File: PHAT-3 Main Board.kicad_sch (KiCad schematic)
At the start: 30 parts, among them P1 Power Terminal Block, P2 Power Terminal Block, P3 Power Terminal Block, P4 Power Terminal Block, Q1 IRLZ44N, SW1 SW_Push_SPDT, U1 AHT21, U10 Logic Level Converter, U2 ESP32-S3 Dual-core SX1262, U3 GY-68 BMP180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

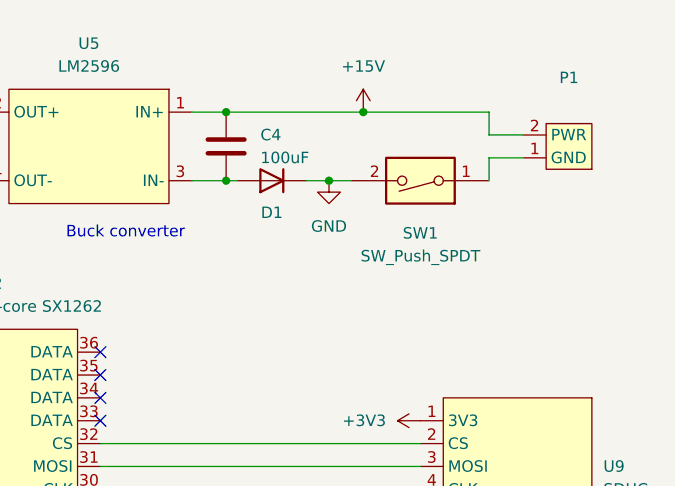
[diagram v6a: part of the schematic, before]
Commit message: Updated Switch and Resistor Placement
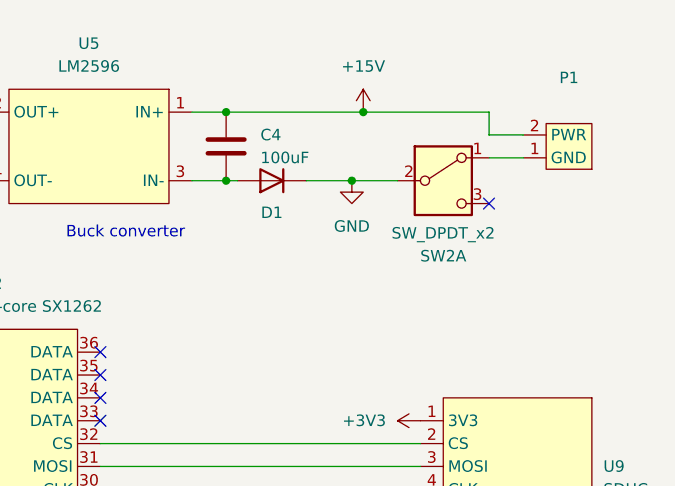
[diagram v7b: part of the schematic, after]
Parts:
- removed SW1: SW_Push_SPDT, Button_Switch_THT:SW_DIP_SPSTx01_Slide_9.78x4.72mm_W7.62mm_P2.54mm, symbol Switch:SW_DIP_x01
- added SW2: SW_DPDT_x2, Button_Switch_THT:SW_Slide-03_Wuerth-WS-SLTV_10x2.5x6.4_P2.54mm, symbol Switch:SW_DPDT_x2
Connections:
- net GND: now also SW2.2 (B)
- net at P1.1 (GND): now also SW2.1 (A)
- no-connect marks 31 -> 32
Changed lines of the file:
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@@
 	)
 	(junction
+		(at 204.47 46.99)
+		(diameter 0)
+		(color 0 0 0 0)
+	)
+	(junction
 		(at 102.87 99.06)
 		(diameter 0)
@@
 	)
 	(junction
-		(at 201.93 46.99)
-		(diameter 0)
-		(color 0 0 0 0)
-	)
-	(junction
 		(at 95.25 96.52)
 		(diameter 0)
@@
 	)
 	(no_connect
+		(at 219.71 49.53)
+	)
+	(no_connect
 		(at 123.19 138.43)
 	)
@@
 	(wire
 		(pts
+			(xy 219.71 44.45) (xy 223.52 44.45)
+		)
+		(stroke
+			(width 0)
+			(type default)
+		)
+	)
+	(wire
+		(pts
 			(xy 107.95 53.34) (xy 107.95 71.12)
 		)
@@
 	(wire
 		(pts
-			(xy 199.39 46.99) (xy 201.93 46.99)
+			(xy 199.39 46.99) (xy 204.47 46.99)
 		)
 		(stroke
@@
 	(wire
 		(pts
-			(xy 219.71 44.45) (xy 223.52 44.45)
-		)
-		(stroke
-			(width 0)
-			(type default)
-		)
-	)
-	(wire
-		(pts
 			(xy 133.35 99.06) (xy 133.35 114.3)
 		)
@@
 	(wire
 		(pts
-			(xy 201.93 46.99) (xy 204.47 46.99)
-		)
-		(stroke
-			(width 0)
-			(type default)
-		)
-	)
-	(wire
-		(pts
 			(xy 135.89 96.52) (xy 152.4 96.52)
 		)
@@
 	(wire
 		(pts
-			(xy 219.71 46.99) (xy 219.71 44.45)
-		)
-		(stroke
-			(width 0)
-			(type default)
-		)
-	)
-	(wire
-		(pts
 			(xy 119.38 73.66) (xy 119.38 93.98)
 		)
@@
 	(wire
 		(pts
+			(xy 204.47 46.99) (xy 209.55 46.99)
+		)
+		(stroke
+			(width 0)
+			(type default)
+		)
+	)
+	(wire
+		(pts
 			(xy 176.53 78.74) (xy 212.09 78.74)
 		)
@@
 	)
 	(symbol
+		(lib_id "Switch:SW_DPDT_x2")
+		(at 214.63 46.99 0)
+		(unit 1)
+		(exclude_from_sim no)
+		(in_bom yes)
+		(on_board yes)
+		(dnp no)
+		(property "Reference" "SW2"
+			(at 214.63 55.372 0)
+			(effects
+				(font
+					(size 1.27 1.27)
+				)
+			)
+		)
+		(property "Value" "SW_DPDT_x2"
+			(at 214.63 52.832 0)
+			(effects
+				(font
+					(size 1.27 1.27)
+				)
+			)
+		)
+		(property "Footprint" "Button_Switch_THT:SW_Slide-03_Wuerth-WS-SLTV_10x2.5x6.4_P2.54mm"
+			(at 214.63 46.99 0)
+			(effects
+				(font
+					(size 1.27 1.27)
+				)
+				(hide yes)
+			)
+		)
+		(property "Datasheet" "~"
+			(at 214.63 46.99 0)
+			(effects
+				(font
+					(size 1.27 1.27)
+				)
+				(hide yes)
+			)
+		)
+		(property "Description" "Switch, dual pole double throw, separate symbols"
+			(at 214.63 46.99 0)
+			(effects
+				(font
+					(size 1.27 1.27)
+				)
+				(hide yes)
+			)
+		)
+		(pin "5"
+		)
+		(pin "1"
+		)
+		(pin "6"
+		)
+		(pin "4"
+		)
+		(pin "3"
+		)
+		(pin "2"
+		)
+		(instances
+			(project ""
+				(path "/da389c8a-9ca2-41c4-a7eb-3ce46ba4333b"
+					(reference "SW2")
+					(unit 1)
+				)
+			)
+		)
+	)
+	(symbol
 		(lib_id "Footprint Library:uCAM-III")
 		(at 113.03 50.8 90)
@@
 	)
 	(symbol
-		(lib_id "Switch:SW_DIP_x01")
-		(at 212.09 46.99 180)
-		(unit 1)
-		(exclude_from_sim no)
-		(in_bom yes)
-		(on_board yes)
-		(dnp no)
-		(property "Reference" "SW1"
-			(at 212.09 52.832 0)
-			(effects
-				(font
-					(size 1.27 1.27)
-				)
-			)
-		)
-		(property "Value" "SW_Push_SPDT"
-			(at 212.09 55.372 0)
-			(effects
-				(font
-					(size 1.27 1.27)
-				)
-			)
-		)
-		(property "Footprint" "Button_Switch_THT:SW_DIP_SPSTx01_Slide_9.78x4.72mm_W7.62mm_P2.54mm"
-			(at 212.09 46.99 0)
-			(effects
-				(font
-					(size 1.27 1.27)
-				)
-				(hide yes)
-			)
-		)
-		(property "Datasheet" "~"
-			(at 212.09 46.99 0)
-			(effects
-				(font
-					(size 1.27 1.27)
-				)
-				(hide yes)
-			)
-		)
-		(property "Description" "1x DIP Switch, Single Pole Single Throw (SPST) switch, small symbol"
-			(at 212.09 46.99 0)
-			(effects
-				(font
-					(size 1.27 1.27)
-				)
-				(hide yes)
-			)
-		)
-		(pin "1"
-		)
-		(pin "2"
-		)
-		(instances
-			(project ""
-				(path "/da389c8a-9ca2-41c4-a7eb-3ce46ba4333b"
-					(reference "SW1")
-					(unit 1)
-				)
-			)
-		)
-	)
-	(symbol
 		(lib_id "power:+3V3")
 		(at 102.87 106.68 180)
@@
 	(symbol
 		(lib_id "power:GND")
-		(at 201.93 46.99 0)
+		(at 204.47 46.99 0)
 		(unit 1)
 		(exclude_from_sim no)
@@
 		(fields_autoplaced yes)
 		(property "Reference" "#PWR031"
-			(at 201.93 53.34 0)
+			(at 204.47 53.34 0)
 			(effects
 				(font
@@
 		)
 		(property "Value" "GND"
-			(at 201.93 52.07 0)
+			(at 204.47 52.07 0)
 			(effects
 				(font
@@
 		)
 		(property "Footprint" ""
-			(at 201.93 46.99 0)
+			(at 204.47 46.99 0)
 			(effects
 				(font
@@
 		)
 		(property "Datasheet" ""
-			(at 201.93 46.99 0)
+			(at 204.47 46.99 0)
 			(effects
 				(font
@@
 		)
 		(property "Description" "Power symbol creates a global label with name \"GND\" , ground"
-			(at 201.93 46.99 0)
+			(at 204.47 46.99 0)
 			(effects
 				(font

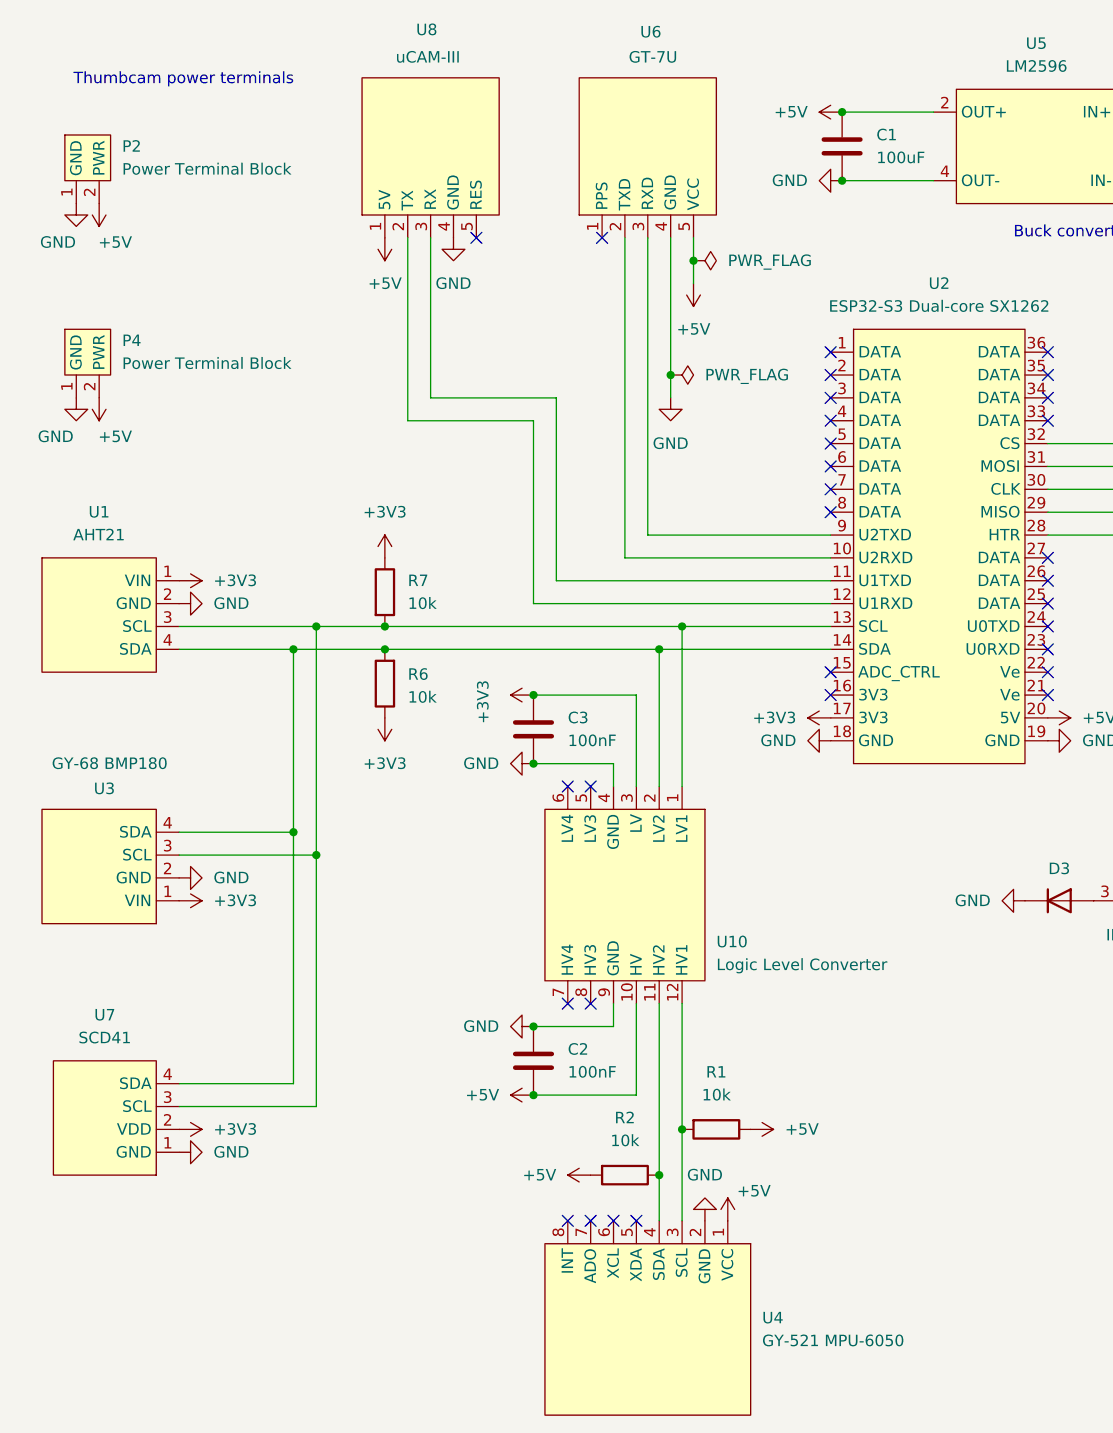
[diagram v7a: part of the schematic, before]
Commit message: Changed UART and I2C Pins
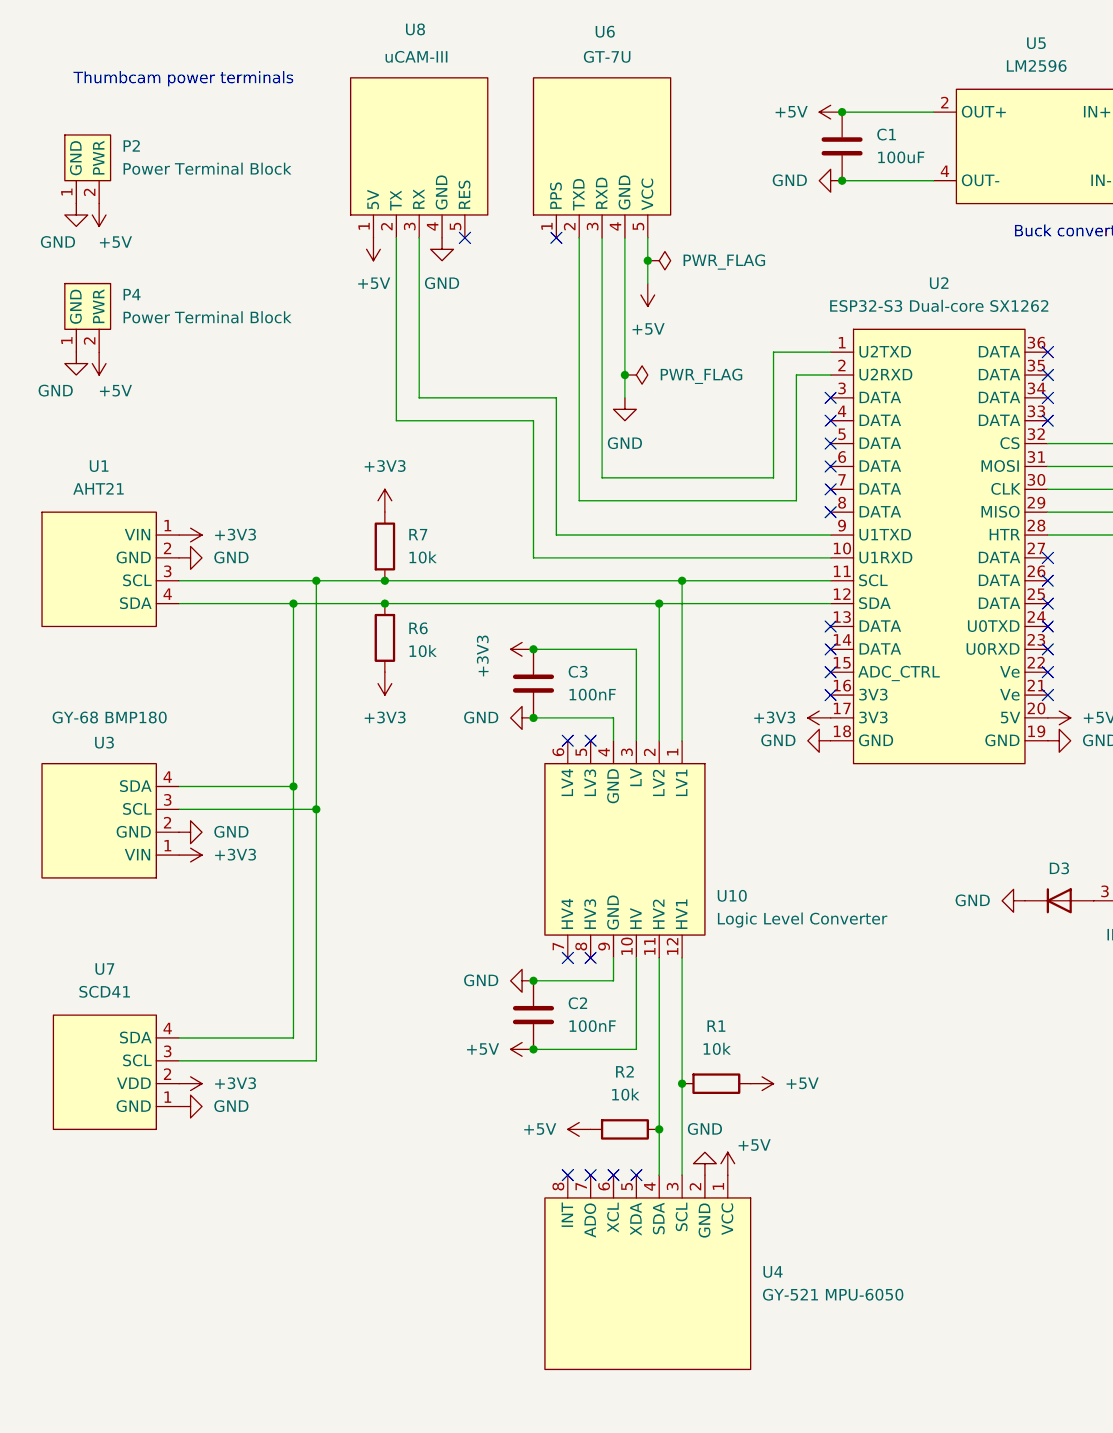
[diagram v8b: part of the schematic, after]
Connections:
- net at U6.2 (TXD): now also U2.2 (U2RXD); no longer U2.10 (U2RXD)
- net at U6.3 (RXD): now also U2.1 (U2TXD); no longer U2.9 (U2TXD)
- net at R7.2, U1.3 (SCL), U10.1 (LV1)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: now also U2.11 (SCL); no longer U2.13 (SCL)
- net at R6.2, U1.4 (SDA), U10.2 (LV2)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: now also U2.12 (SDA); no longer U2.14 (SDA)
- net at U8.3 (RX): now also U2.9 (U1TXD); no longer U2.11 (U1TXD)
- net at U8.2 (TX): now also U2.10 (U1RXD); no longer U2.12 (U1RXD)
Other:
- moved on the sheet: C2, C3, P4, R1, R2, R6, R7, U1, U10, U3, U4, U6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
